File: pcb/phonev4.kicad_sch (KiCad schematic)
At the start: 37 parts, among them J1 coin, J2 keypad, J3 display, J4 RJ9, J5 mic, J6 card_reader, J7 speaker, Q1 Si2319CDS, U2 TDA2822M

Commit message: pcb: Rename power nets 5v→5V_MAIN, 12v→12V_COIN (fixes #69)
- Schematic: global_label and TP1 Value
- PCB: net definitions, pads, pour zone net_name

Co-authored-by: Cursor <cursoragent@cursor.com>
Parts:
- TP1: value 5v -> 5V_MAIN
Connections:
- net 12v renamed 12V_COIN
- net 5v renamed 5V_MAIN
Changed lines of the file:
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@@
 		)
 	)
-	(global_label "5v"
+	(global_label "5V_MAIN"
 		(shape input)
 		(at 40.64 134.62 180)
@@
 		)
 	)
-	(global_label "5v"
+	(global_label "5V_MAIN"
 		(shape input)
 		(at 119.38 -3.81 0)
@@
 		)
 	)
-	(global_label "5v"
+	(global_label "5V_MAIN"
 		(shape input)
 		(at 92.71 186.69 0)
@@
 		)
 	)
-	(global_label "5v"
+	(global_label "5V_MAIN"
 		(shape input)
 		(at 63.5 40.64 180)
@@
 		)
 	)
-	(global_label "5v"
+	(global_label "5V_MAIN"
 		(shape input)
 		(at 113.03 125.73 0)
@@
 		)
 	)
-	(global_label "5v"
+	(global_label "5V_MAIN"
 		(shape input)
 		(at 271.78 34.29 0)
@@
 		)
 	)
-	(global_label "5v"
+	(global_label "5V_MAIN"
 		(shape input)
 		(at 292.1 31.75 0)
@@
 		)
 	)
-	(global_label "5v"
+	(global_label "5V_MAIN"
 		(shape input)
 		(at 237.49 22.86 0)
@@
 		)
 	)
-	(global_label "12v"
+	(global_label "12V_COIN"
 		(shape input)
 		(at 261.62 49.53 0)
@@
 		)
 	)
-	(global_label "12v"
+	(global_label "12V_COIN"
 		(shape input)
 		(at 113.03 40.64 180)
@@
 		)
 	)
-	(global_label "5v"
+	(global_label "5V_MAIN"
 		(shape input)
 		(at 299.72 59.69 0)
@@
 		)
 	)
-	(global_label "5v"
+	(global_label "5V_MAIN"
 		(shape input)
 		(at 119.38 214.63 0)
@@
 		)
 	)
-	(global_label "5v"
+	(global_label "5V_MAIN"
 		(shape input)
 		(at 39.37 102.87 180)
@@
 		)
 	)
-	(global_label "5v"
+	(global_label "5V_MAIN"
 		(shape input)
 		(at 147.32 101.6 180)
@@
 			)
 		)
-		(property "Value" "5v"
+		(property "Value" "5V_MAIN"
 			(at 294.64 29.7179 0)
 			(effects

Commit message: pcb: Assign missing footprints for D3, F1, TP1–TP5 (fixes #72)
- D3 (power LED): LED_SMD:LED_0805_2012Metric
- F1 (1A PTC): Fuse:Fuse_1812_4532Metric_Pad1.30x3.40mm_HandSolder
- TP1–TP5: TestPoint:TestPoint_Pad_D1.5mm

Run 'Update PCB from Schematic' in KiCad to apply to board.

Co-authored-by: Cursor <cursoragent@cursor.com>
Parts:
- D3: footprint (none) -> LED_SMD:LED_0805_2012Metric
- F1: footprint (none) -> Fuse:Fuse_1812_4532Metric_Pad1.30x3.40mm_HandSolder
- TP1, TP2, TP3, TP4, TP5: footprint (none) -> TestPoint:TestPoint_Pad_D1.5mm
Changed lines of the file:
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@@
 			)
 		)
-		(property "Footprint" ""
+		(property "Footprint" "TestPoint:TestPoint_Pad_D1.5mm"
 			(at 297.18 31.75 0)
 			(effects
@@
 			)
 		)
-		(property "Footprint" ""
+		(property "Footprint" "TestPoint:TestPoint_Pad_D1.5mm"
 			(at 22.86 186.69 0)
 			(effects
@@
 			)
 		)
-		(property "Footprint" ""
+		(property "Footprint" "Fuse:Fuse_1812_4532Metric_Pad1.30x3.40mm_HandSolder"
 			(at 267.97 32.512 90)
 			(effects
@@
 			)
 		)
-		(property "Footprint" ""
+		(property "Footprint" "TestPoint:TestPoint_Pad_D1.5mm"
 			(at 92.71 241.3 0)
 			(effects
@@
 			)
 		)
-		(property "Footprint" ""
+		(property "Footprint" "TestPoint:TestPoint_Pad_D1.5mm"
 			(at 54.61 149.86 0)
 			(effects
@@
 			)
 		)
-		(property "Footprint" ""
+		(property "Footprint" "TestPoint:TestPoint_Pad_D1.5mm"
 			(at 46.99 139.7 0)
 			(effects
@@
 			)
 		)
-		(property "Footprint" ""
+		(property "Footprint" "LED_SMD:LED_0805_2012Metric"
 			(at 119.38 226.06 0)
 			(effects

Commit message: pcb: Prefer through-hole footprints for D3, F1, TP1–TP5
- D3 (LED): LED_SMD 0805 → LED_THT 5mm round
- F1 (fuse): Fuse 1812 SMD → Fuse_Radial D10mm THT
- TP1–TP5: TestPoint SMD pad → TestPoint Loop D2.5mm THT

Update README BOM table and LED refs (LED1→D3).

Co-authored-by: Cursor <cursoragent@cursor.com>
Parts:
- D3: footprint LED_SMD:LED_0805_2012Metric -> LED_THT:LED_D5.0mm
- F1: footprint Fuse:Fuse_1812_4532Metric_Pad1.30x3.40mm_HandSolder -> Fuse:Fuse_Radial_D10.0mm_P5.00mm
- TP1, TP2, TP3, TP4, TP5: footprint TestPoint:TestPoint_Pad_D1.5mm -> TestPoint:TestPoint_Loop_D2.50mm_Drill1.0mm
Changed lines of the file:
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@@
 			)
 		)
-		(property "Footprint" "TestPoint:TestPoint_Pad_D1.5mm"
+		(property "Footprint" "TestPoint:TestPoint_Loop_D2.50mm_Drill1.0mm"
 			(at 297.18 31.75 0)
 			(effects
@@
 			)
 		)
-		(property "Footprint" "TestPoint:TestPoint_Pad_D1.5mm"
+		(property "Footprint" "TestPoint:TestPoint_Loop_D2.50mm_Drill1.0mm"
 			(at 22.86 186.69 0)
 			(effects
@@
 			)
 		)
-		(property "Footprint" "Fuse:Fuse_1812_4532Metric_Pad1.30x3.40mm_HandSolder"
+		(property "Footprint" "Fuse:Fuse_Radial_D10.0mm_P5.00mm"
 			(at 267.97 32.512 90)
 			(effects
@@
 			)
 		)
-		(property "Footprint" "TestPoint:TestPoint_Pad_D1.5mm"
+		(property "Footprint" "TestPoint:TestPoint_Loop_D2.50mm_Drill1.0mm"
 			(at 92.71 241.3 0)
 			(effects
@@
 			)
 		)
-		(property "Footprint" "TestPoint:TestPoint_Pad_D1.5mm"
+		(property "Footprint" "TestPoint:TestPoint_Loop_D2.50mm_Drill1.0mm"
 			(at 54.61 149.86 0)
 			(effects
@@
 			)
 		)
-		(property "Footprint" "TestPoint:TestPoint_Pad_D1.5mm"
+		(property "Footprint" "TestPoint:TestPoint_Loop_D2.50mm_Drill1.0mm"
 			(at 46.99 139.7 0)
 			(effects
@@
 			)
 		)
-		(property "Footprint" "LED_SMD:LED_0805_2012Metric"
+		(property "Footprint" "LED_THT:LED_D5.0mm"
 			(at 119.38 226.06 0)
 			(effects

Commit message: pcb: Use P3.80mm for 100µF radial caps per Digi-Key availability
100µF 16V 8mm parts use 3.5–5mm pitch; P2mm uncommon. Schematic had
P2.00mm (not in KiCad lib); PCB already uses P3.80mm. Restore P3.80mm
for schematic/BOM/README. Add Digi-Key research notes to AUDIT.md.

Co-authored-by: Cursor <cursoragent@cursor.com>
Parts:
- C_outA, C_outB, C_vcc: footprint Capacitor_THT:CP_Radial_D8.0mm_P2.00mm -> Capacitor_THT:CP_Radial_D8.0mm_P3.80mm
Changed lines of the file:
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@@
 			)
 		)
-		(property "Footprint" "Capacitor_THT:CP_Radial_D8.0mm_P2.00mm"
+		(property "Footprint" "Capacitor_THT:CP_Radial_D8.0mm_P3.80mm"
 			(at 113.03 146.05 0)
 			(effects
@@
 			)
 		)
-		(property "Footprint" "Capacitor_THT:CP_Radial_D8.0mm_P2.00mm"
+		(property "Footprint" "Capacitor_THT:CP_Radial_D8.0mm_P3.80mm"
 			(at 137.16 146.05 0)
 			(effects
@@
 			)
 		)
-		(property "Footprint" "Capacitor_THT:CP_Radial_D8.0mm_P2.00mm"
+		(property "Footprint" "Capacitor_THT:CP_Radial_D8.0mm_P3.80mm"
 			(at 137.16 156.21 0)
 			(effects

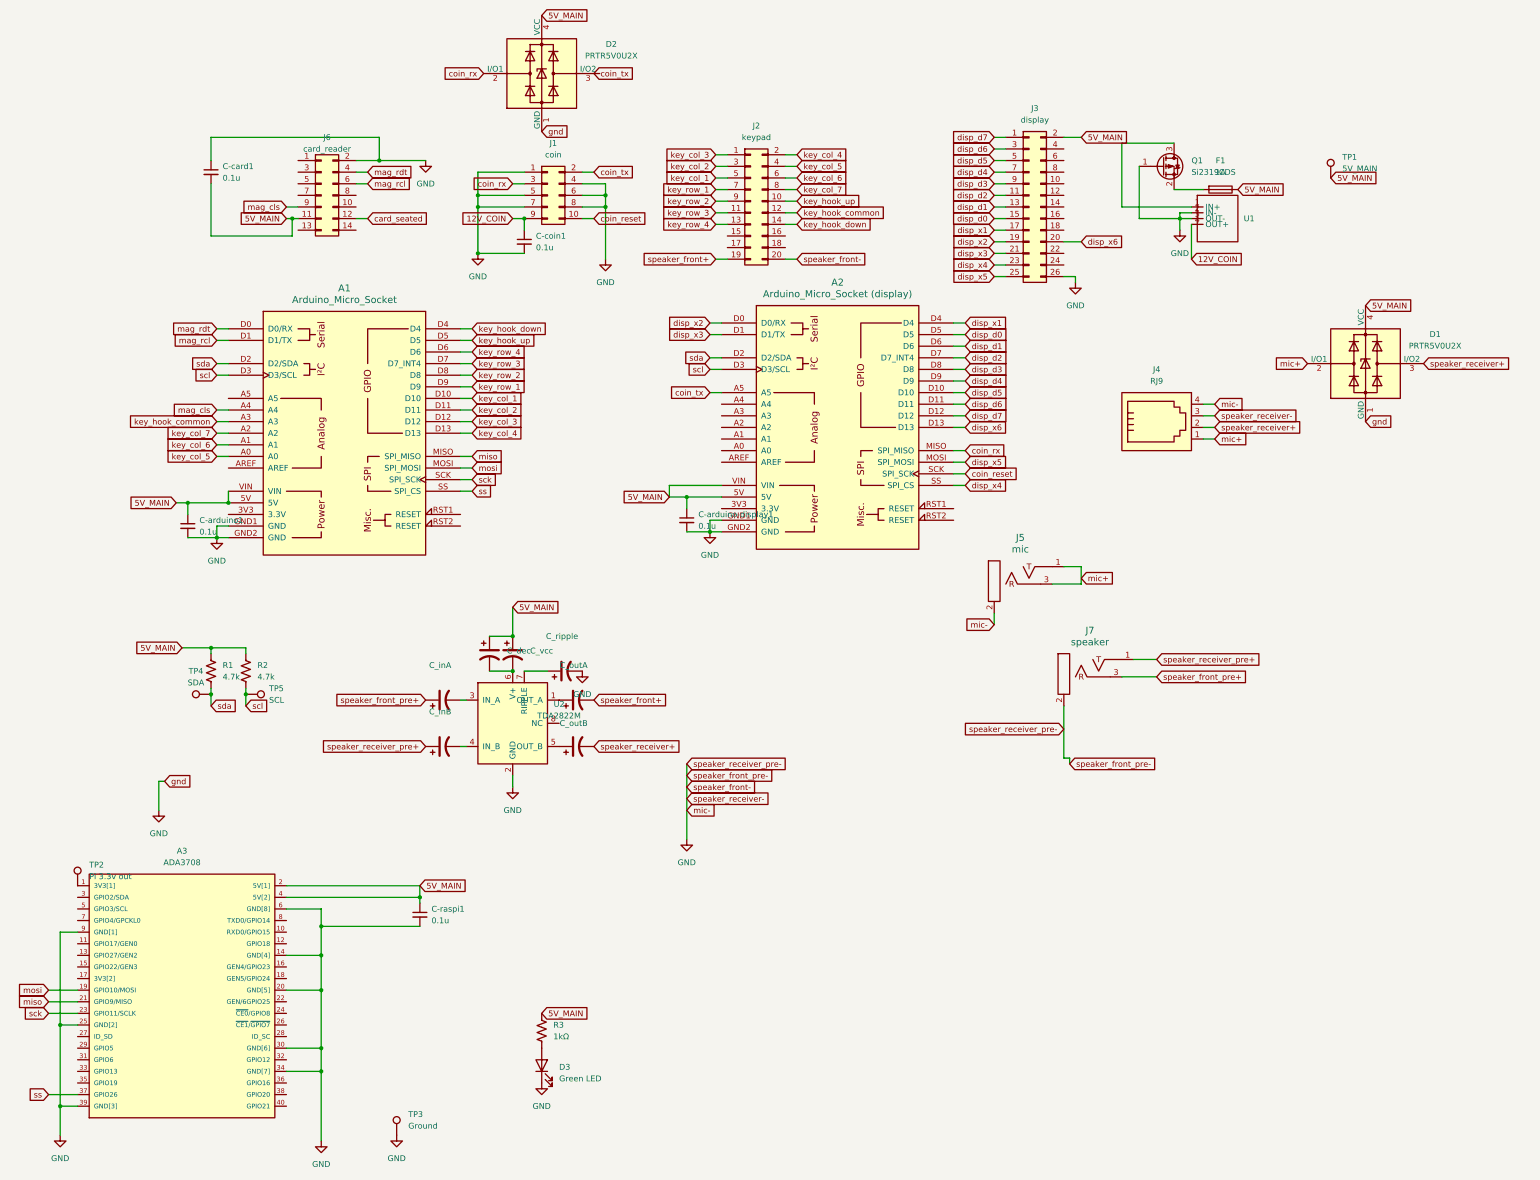
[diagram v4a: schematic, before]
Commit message: PCB: schematic cleanup, cap renames C1-C12, F1 footprint fix, docs
- Rename capacitors to standard refs (C1-C12): C-arduino1->C1, C_inA1->C9, etc.
- F1 footprint: use Capacitor_THT:CP_Radial_D10.0mm_P5.00mm (Fuse_Radial missing in KiCad)
- UNUSED_PINS.md: D2 pin 3 now used (coin_tx)
- SCHEMATIC_LAYOUT.md: layout guide for subsections
- AUDIT.md: wiring verification checked, ERC count 154
- BOM_CHECK.md, phonev4.csv: align with new refs

Co-authored-by: Cursor <cursoragent@cursor.com>
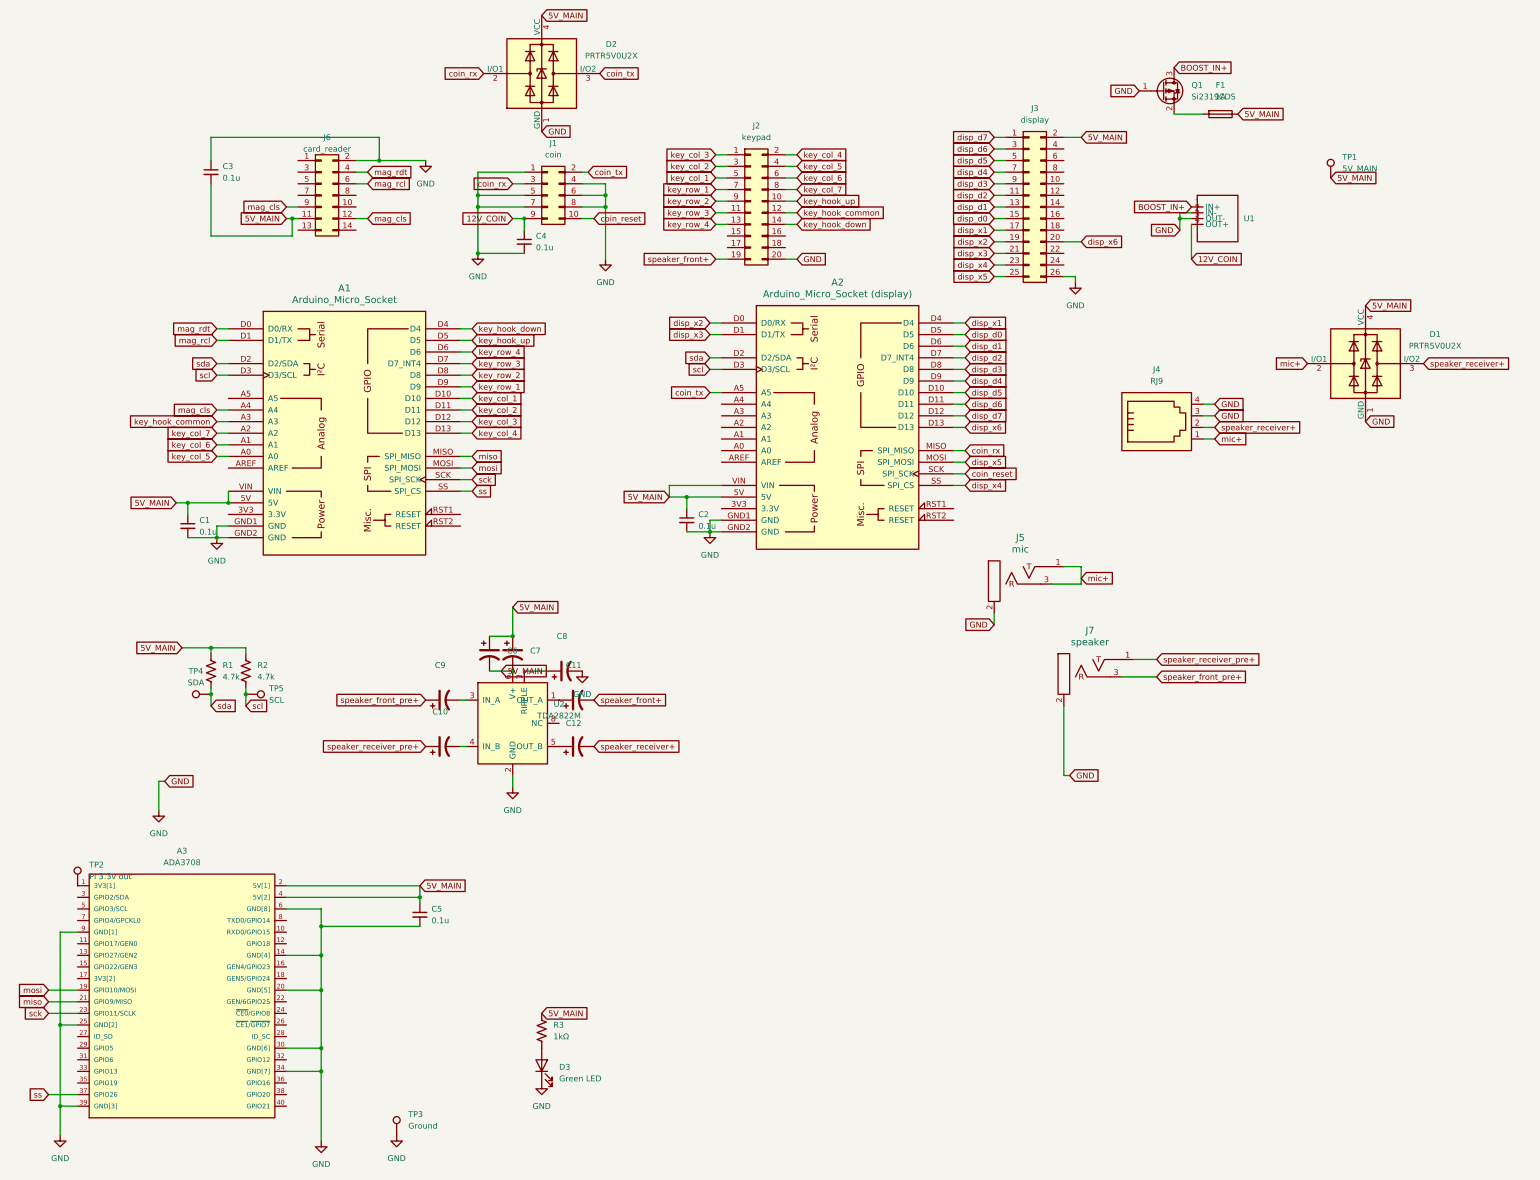
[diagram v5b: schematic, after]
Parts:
- F1: footprint Fuse:Fuse_Radial_D10.0mm_P5.00mm -> Capacitor_THT:CP_Radial_D10.0mm_P5.00mm
- renumbered C-arduino1 to C1, C_inB to C10, C_outA to C11, C_outB to C12, C-arduino-display1 to C2, C-card1 to C3, C-coin1 to C4, C-raspi1 to C5, C_dec to C6, C_vcc to C7, C_ripple to C8, C_inA to C9
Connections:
- net card_seated is gone; now on net mag_cls: J6.12 (Pin_12)
- net 5V_MAIN: now also C6.2, C7.2, U2.6 (V+)
- net coin_tx: now also D2.3 (I/O2)
- net BOOST_IN+: now reaches Q1.3 (D), U1.1 (IN+)
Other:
- moved on the sheet: F1, Q1
